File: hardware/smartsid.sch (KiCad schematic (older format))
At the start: 64 parts, among them P1 INPUT, P2 CONTROL, P3 POT2, P4 SOCKET LEFT, P5 OUTPUT, P6 SOCKET RIGHT, Q1 BC547, Q2 BC547, U1 GAL16V8, U2 SID2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

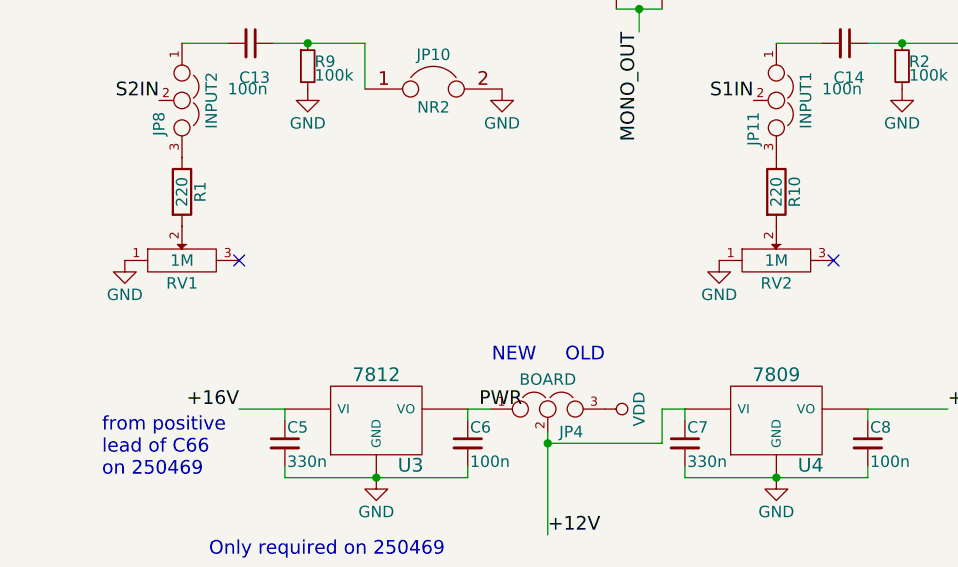
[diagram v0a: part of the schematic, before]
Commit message: Hardware: Improved silkscreen, corrected pot refs
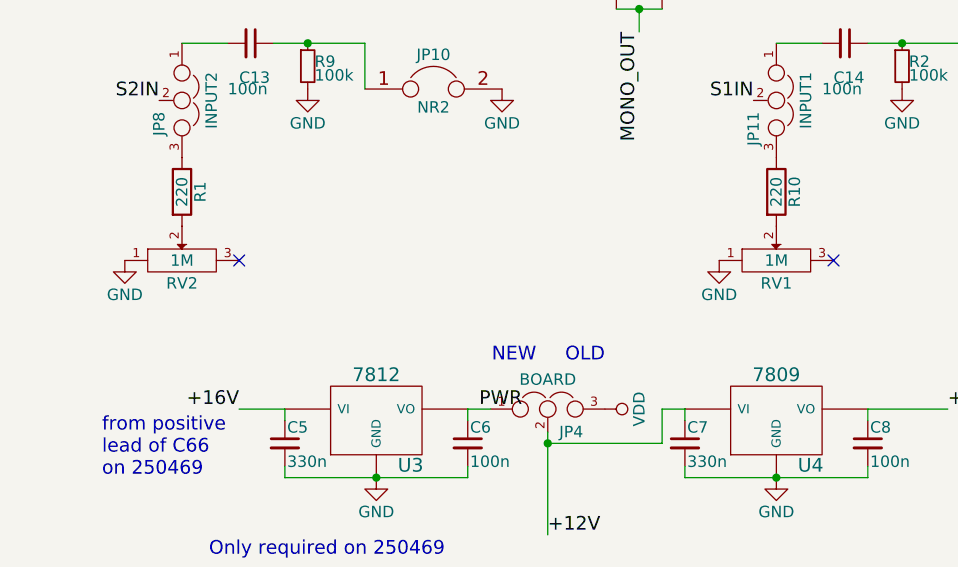
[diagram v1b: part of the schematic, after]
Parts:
- P1: footprint Pin_Headers:Pin_Header_Straight_1x05 -> Pinheaders:Pin_Header_Straight_1x05
- P2: footprint Pin_Headers:Pin_Header_Straight_2x06 -> Pinheaders:Pin_Header_Straight_2x06
- renumbered RV2 to RV1, RV1 to RV2
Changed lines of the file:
@@
 F 0 "P1" H 1250 1400 50  0000 C CNN
 F 1 "INPUT" V 1350 1100 50  0000 C CNN
-F 2 "Pin_Headers:Pin_Header_Straight_1x05" H 1250 1100 60  0001 C CNN
+F 2 "Pinheaders:Pin_Header_Straight_1x05" H 1250 1100 60  0001 C CNN
 F 3 "" H 1250 1100 60  0000 C CNN
 	1    1250 1100
@@
 $EndComp
 $Comp
-L POT RV2
+L POT RV1
 U 1 1 56E2B1AB
 P 5150 6300
-F 0 "RV2" H 5150 6200 50  0000 C CNN
+F 0 "RV1" H 5150 6200 50  0000 C CNN
 F 1 "1M" H 5150 6300 50  0000 C CNN
 F 2 "Potentiometers:Potentiometer_Bourns_3296W_3-8Zoll_Inline_ScrewUp" H 5150 6300 60  0001 C CNN
@@
 $EndComp
 $Comp
-L POT RV1
+L POT RV2
 U 1 1 56E2E530
 P 2550 6300
-F 0 "RV1" H 2550 6200 50  0000 C CNN
+F 0 "RV2" H 2550 6200 50  0000 C CNN
 F 1 "1M" H 2550 6300 50  0000 C CNN
 F 2 "Potentiometers:Potentiometer_Bourns_3296W_3-8Zoll_Inline_ScrewUp" H 2550 6300 60  0001 C CNN
@@
 F 0 "P2" H 1200 2350 50  0000 C CNN
 F 1 "CONTROL" H 1200 1650 50  0000 C CNN
-F 2 "Pin_Headers:Pin_Header_Straight_2x06" H 1200 800 60  0001 C CNN
+F 2 "Pinheaders:Pin_Header_Straight_2x06" H 1200 800 60  0001 C CNN
 F 3 "" H 1200 800 60  0000 C CNN
 	1    1200 2000

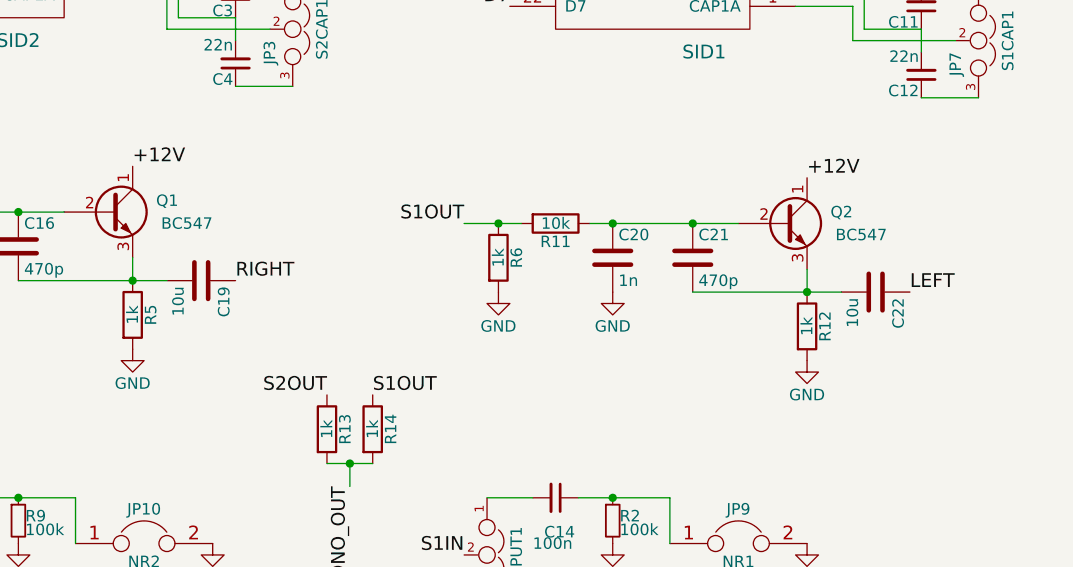
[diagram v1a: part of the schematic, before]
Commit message: Hardware: Fixed decoupling caps (now polarized), removed gerbers
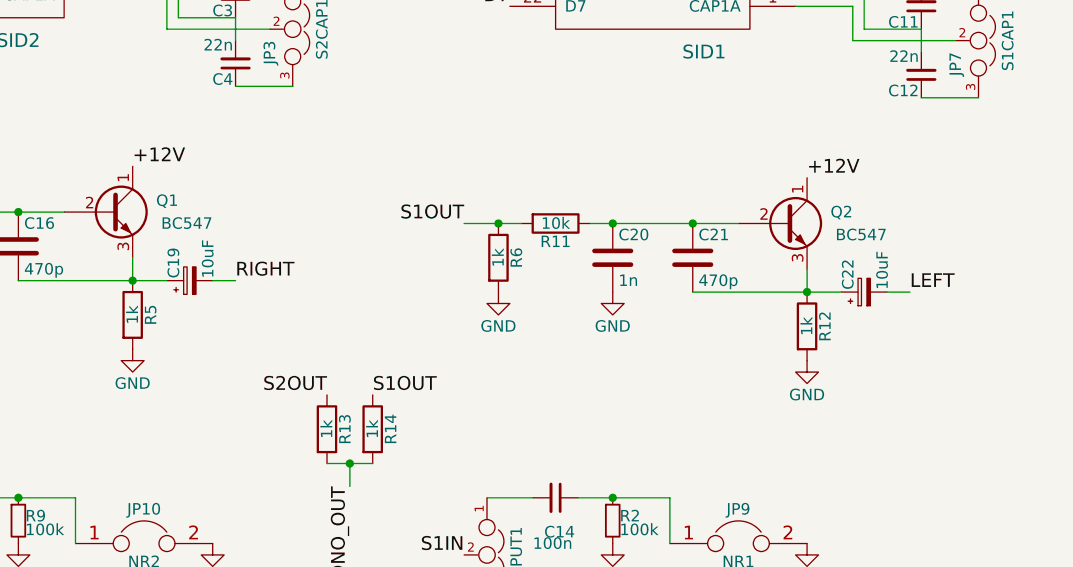
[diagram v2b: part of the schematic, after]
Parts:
- removed C19, C22: 10u, Capacitors_ThroughHole:C_Radial_D5_L6_P2.5, symbol C
- added C19, C22: 10uF, Capacitors_ThroughHole:C_Radial_D5_L6_P2.5, symbol CP_Small
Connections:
- net LEFT: now also C22.2
- net RIGHT: now also C19.2
- net at C16.2, Q1.3 (E), R5.1: now also C19.1
- net at C21.2, Q2.3 (E), R12.1: now also C22.1
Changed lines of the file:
@@
 	1    0    0    -1
-$EndComp
-$Comp
-L C C19
-U 1 1 56E6C289
-P 3900 4400
-F 0 "C19" H 3925 4500 50  0000 L CNN
-F 1 "10u" H 3925 4300 50  0000 L CNN
-F 2 "Capacitors_ThroughHole:C_Radial_D5_L6_P2.5" H 3938 4250 30  0001 C CNN
-F 3 "" H 3900 4400 60  0000 C CNN
-	1    3900 4400
-	0    1    1    0
 $EndComp
 Connection ~ 3600 4400
@@
 	1    5700 4450
 	1    0    0    -1
-$EndComp
-$Comp
-L C C22
-U 1 1 56E6CA65
-P 6850 4450
-F 0 "C22" H 6875 4550 50  0000 L CNN
-F 1 "10u" H 6875 4350 50  0000 L CNN
-F 2 "Capacitors_ThroughHole:C_Radial_D5_L6_P2.5" H 6888 4300 30  0001 C CNN
-F 3 "" H 6850 4450 60  0000 C CNN
-	1    6850 4450
-	0    1    1    0
 $EndComp
 Connection ~ 6550 4450
@@
 	1    0    0    -1
 $EndComp
+$Comp
+L CP_Small C19
+U 1 1 5707E4A7
+P 3850 4400
+F 0 "C19" H 3860 4470 50  0000 L CNN
+F 1 "10uF" H 3860 4320 50  0000 L CNN
+F 2 "Capacitors_ThroughHole:C_Radial_D5_L6_P2.5" H 3850 4400 60  0001 C CNN
+F 3 "" H 3850 4400 60  0000 C CNN
+	1    3850 4400
+	0    -1   -1   0
+$EndComp
+Wire Wire Line
+	3950 4400 4050 4400
+$Comp
+L CP_Small C22
+U 1 1 5707EED3
+P 6800 4450
+F 0 "C22" H 6810 4520 50  0000 L CNN
+F 1 "10uF" H 6810 4370 50  0000 L CNN
+F 2 "Capacitors_ThroughHole:C_Radial_D5_L6_P2.5" H 6800 4450 60  0001 C CNN
+F 3 "" H 6800 4450 60  0000 C CNN
+	1    6800 4450
+	0    -1   -1   0
+$EndComp
+Wire Wire Line
+	6900 4450 7000 4450
 $EndSCHEMATC

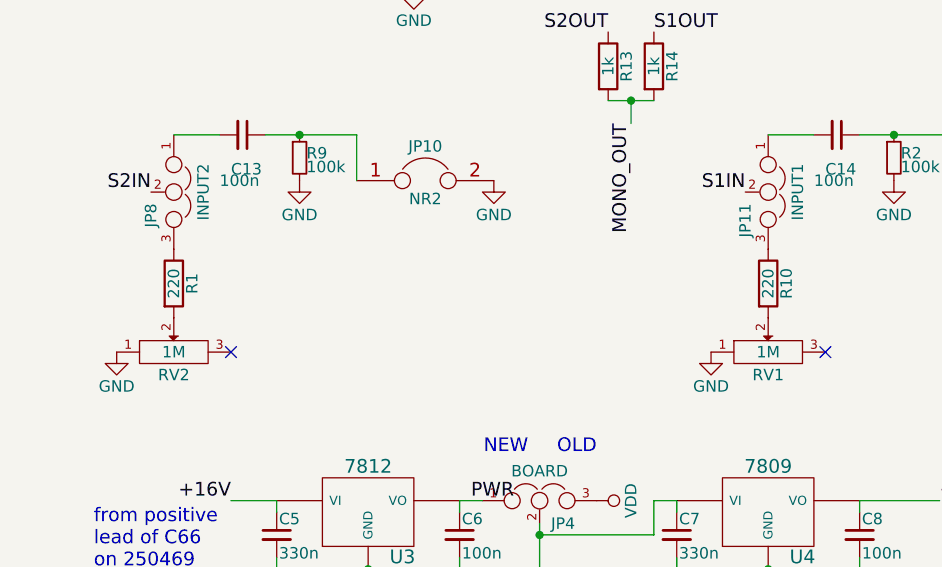
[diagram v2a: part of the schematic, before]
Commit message: Hardware: Fixed values of digifix safety resistors (220k instead of 200)
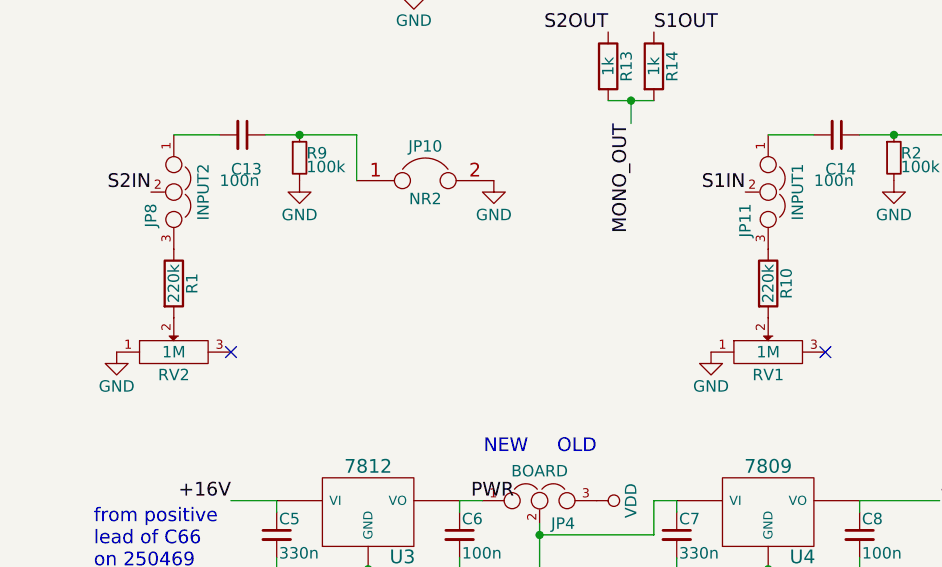
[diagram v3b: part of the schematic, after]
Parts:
- R1, R10: value 220 -> 220k
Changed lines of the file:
@@
 P 5150 6000
 F 0 "R10" V 5230 6000 50  0000 C CNN
-F 1 "220" V 5150 6000 50  0000 C CNN
+F 1 "220k" V 5150 6000 50  0000 C CNN
 F 2 "Discret:R1" V 5080 6000 30  0001 C CNN
 F 3 "" H 5150 6000 30  0000 C CNN
@@
 P 2550 6000
 F 0 "R1" V 2630 6000 50  0000 C CNN
-F 1 "220" V 2550 6000 50  0000 C CNN
+F 1 "220k" V 2550 6000 50  0000 C CNN
 F 2 "Discret:R1" V 2480 6000 30  0001 C CNN
 F 3 "" H 2550 6000 30  0000 C CNN

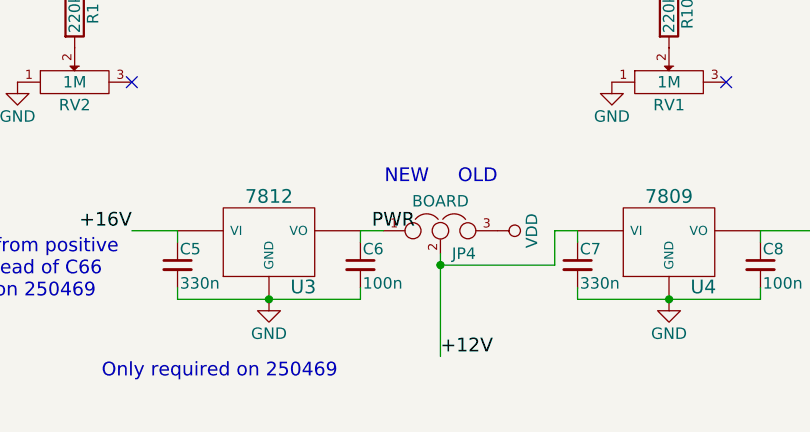
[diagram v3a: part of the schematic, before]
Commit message: Hardware: Adjusted regulator bypass cap values to 470p
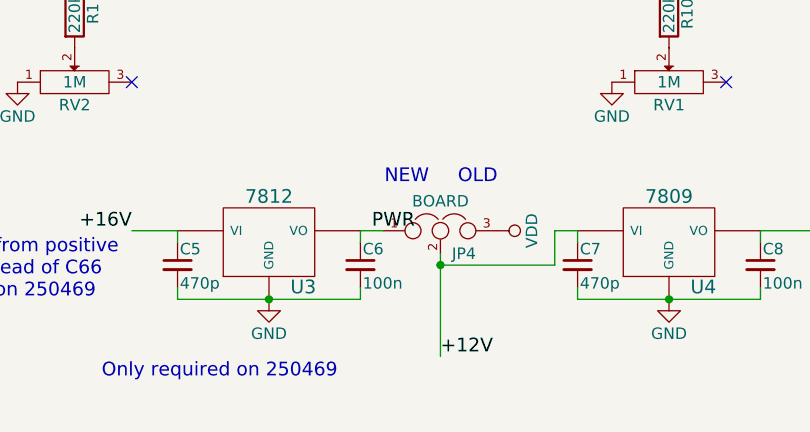
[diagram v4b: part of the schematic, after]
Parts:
- C5, C7: value 330n -> 470p
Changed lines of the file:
@@
 P 3000 7100
 F 0 "C5" H 3010 7170 50  0000 L CNN
-F 1 "330n" H 3010 7020 50  0000 L CNN
+F 1 "470p" H 3010 7020 50  0000 L CNN
 F 2 "Capacitors_ThroughHole:C_Disc_D3_P2.5" H 3000 7100 60  0001 C CNN
 F 3 "" H 3000 7100 60  0000 C CNN
@@
 P 4750 7100
 F 0 "C7" H 4760 7170 50  0000 L CNN
-F 1 "330n" H 4760 7020 50  0000 L CNN
+F 1 "470p" H 4760 7020 50  0000 L CNN
 F 2 "Capacitors_ThroughHole:C_Disc_D3_P2.5" H 4750 7100 60  0001 C CNN
 F 3 "" H 4750 7100 60  0000 C CNN

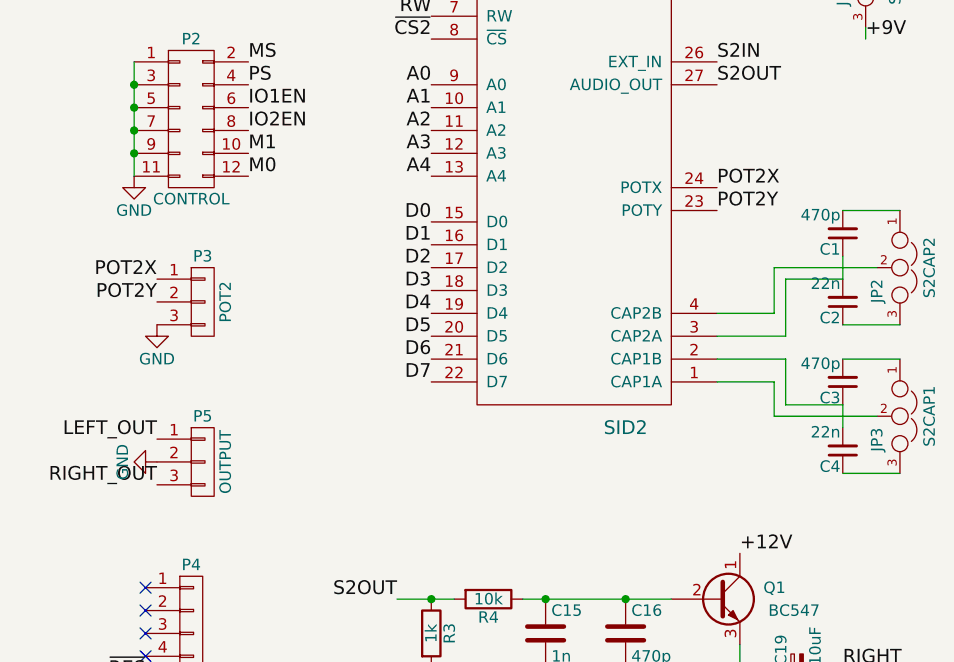
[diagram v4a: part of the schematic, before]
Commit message: Hardware: Removed SID2 pot connector, moved board select jumper
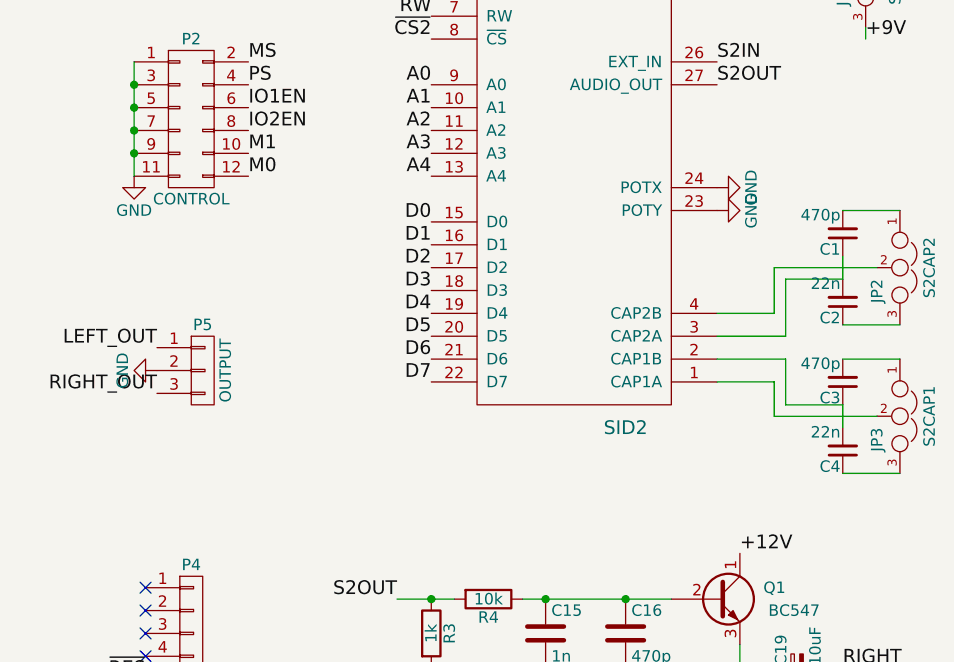
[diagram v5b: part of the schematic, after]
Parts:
- removed P3: POT2, Pinheaders:Pin_Header_Straight_1x03, symbol CONN_01X03
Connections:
- net POT2X is gone; now on net GND: U2.24 (POTX)
- net POT2Y is gone; now on net GND: U2.23 (POTY)
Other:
- moved on the sheet: P5
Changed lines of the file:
@@
 L CONN_01X03 P5
 U 1 1 56DA6151
-P 1250 3500
-F 0 "P5" H 1250 3700 50  0000 C CNN
-F 1 "OUTPUT" V 1350 3500 50  0000 C CNN
-F 2 "Pinheaders:Pin_Header_Straight_1x03" H 1250 3500 60  0001 C CNN
-F 3 "" H 1250 3500 60  0000 C CNN
-	1    1250 3500
+P 1250 3100
+F 0 "P5" H 1250 3300 50  0000 C CNN
+F 1 "OUTPUT" V 1350 3100 50  0000 C CNN
+F 2 "Pinheaders:Pin_Header_Straight_1x03" H 1250 3100 60  0001 C CNN
+F 3 "" H 1250 3100 60  0000 C CNN
+	1    1250 3100
 	1    0    0    -1
 $EndComp
@@
 L GND #PWR011
 U 1 1 56DA641A
-P 1050 3500
-F 0 "#PWR011" H 1050 3250 50  0001 C CNN
-F 1 "GND" H 1050 3350 50  0000 C CNN
-F 2 "" H 1050 3500 60  0000 C CNN
-F 3 "" H 1050 3500 60  0000 C CNN
-	1    1050 3500
+P 1050 3100
+F 0 "#PWR011" H 1050 2850 50  0001 C CNN
+F 1 "GND" H 1050 2950 50  0000 C CNN
+F 2 "" H 1050 3100 60  0000 C CNN
+F 3 "" H 1050 3100 60  0000 C CNN
+	1    1050 3100
 	0    1    1    0
 $EndComp
@@
 Text Label 8650 5450 2    60   ~ 0
 LEFT
-Text Label 1050 3400 2    60   ~ 0
+Text Label 1050 3000 2    60   ~ 0
 LEFT_OUT
-Text Label 1050 3600 2    60   ~ 0
+Text Label 1050 3200 2    60   ~ 0
 RIGHT_OUT
 $Comp
@@
 Connection ~ 950  2050
 Connection ~ 950  2150
-Text Label 3500 2400 0    60   ~ 0
-POT2Y
-Text Label 3500 2300 0    60   ~ 0
-POT2X
-Text Label 1050 2800 2    60   ~ 0
-POT2Y
-Text Label 1050 2700 2    60   ~ 0
-POT2X
-$Comp
-L GND #PWR032
-U 1 1 56D8560C
-P 1050 2900
-F 0 "#PWR032" H 1050 2650 50  0001 C CNN
-F 1 "GND" H 1050 2750 50  0000 C CNN
-F 2 "" H 1050 2900 60  0000 C CNN
-F 3 "" H 1050 2900 60  0000 C CNN
-	1    1050 2900
-	1    0    0    -1
-$EndComp
-$Comp
-L CONN_01X03 P3
-U 1 1 56D85522
-P 1250 2800
-F 0 "P3" H 1250 3000 50  0000 C CNN
-F 1 "POT2" V 1350 2800 50  0000 C CNN
-F 2 "Pinheaders:Pin_Header_Straight_1x03" H 1250 2800 60  0001 C CNN
-F 3 "" H 1250 2800 60  0000 C CNN
-	1    1250 2800
-	1    0    0    -1
-$EndComp
 Text Label 4450 4900 2    60   ~ 0
 S2OUT
@@
 Wire Wire Line
 	6900 4450 7000 4450
+$Comp
+L GND #PWR?
+U 1 1 570B5EB9
+P 3500 2300
+F 0 "#PWR?" H 3500 2050 50  0001 C CNN
+F 1 "GND" H 3500 2150 50  0000 C CNN
+F 2 "" H 3500 2300 60  0000 C CNN
+F 3 "" H 3500 2300 60  0000 C CNN
+	1    3500 2300
+	0    -1   -1   0
+$EndComp
+$Comp
+L GND #PWR?
+U 1 1 570B5F8B
+P 3500 2400
+F 0 "#PWR?" H 3500 2150 50  0001 C CNN
+F 1 "GND" H 3500 2250 50  0000 C CNN
+F 2 "" H 3500 2400 60  0000 C CNN
+F 3 "" H 3500 2400 60  0000 C CNN
+	1    3500 2400
+	0    -1   -1   0
+$EndComp
 $EndSCHEMATC
